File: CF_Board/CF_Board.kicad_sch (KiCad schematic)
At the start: 23 parts, among them J1 Conn_02x04_Odd_Even, SW1 SW_DIP_x08, U1 74FCT16245, U2 74HCT245, U3 22V10, U4 74HCT688, U5 74HCT138, U6 74LVC1G07, X1 DIN41612_03x32_ABC_VMEbus

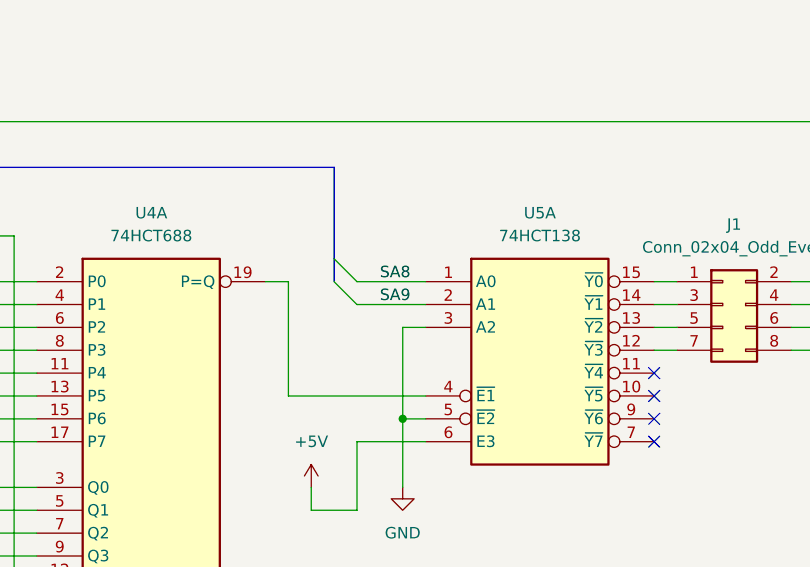
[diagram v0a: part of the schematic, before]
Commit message: Change address decoding to 4KB blocks
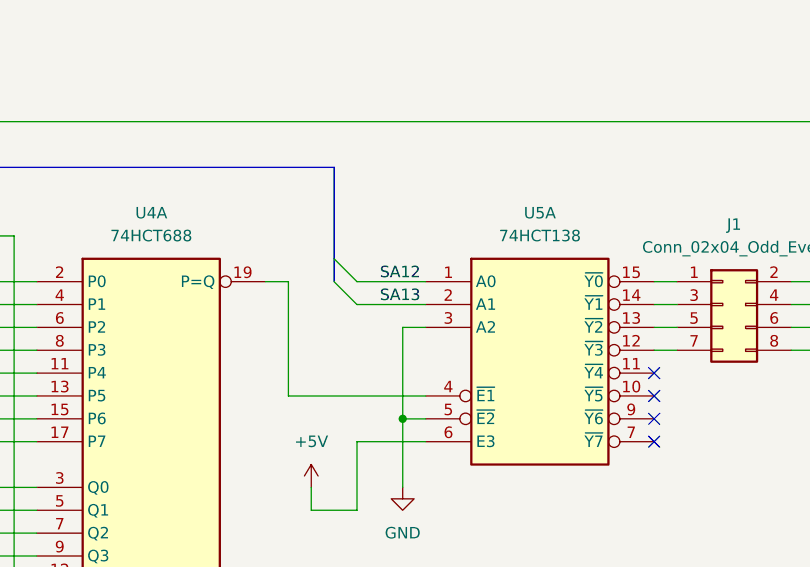
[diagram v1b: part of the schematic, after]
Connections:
- net SA8: no longer U5.1 (A0)
- net SA9: no longer U5.2 (A1)
- new net SA12: U5.1 (A0)
- new net SA13: U5.2 (A1)
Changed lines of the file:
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@@
     (effects (font (size 1.27 1.27)) (justify right bottom))
   )
-  (label "SA9" (at 266.7 167.64 0)
+  (label "SA13" (at 266.7 167.64 0)
     (effects (font (size 1.27 1.27)) (justify left bottom))
   )
@@
     (effects (font (size 1.27 1.27)) (justify left bottom))
   )
-  (label "SA8" (at 266.7 165.1 0)
+  (label "SA12" (at 266.7 165.1 0)
     (effects (font (size 1.27 1.27)) (justify left bottom))
   )

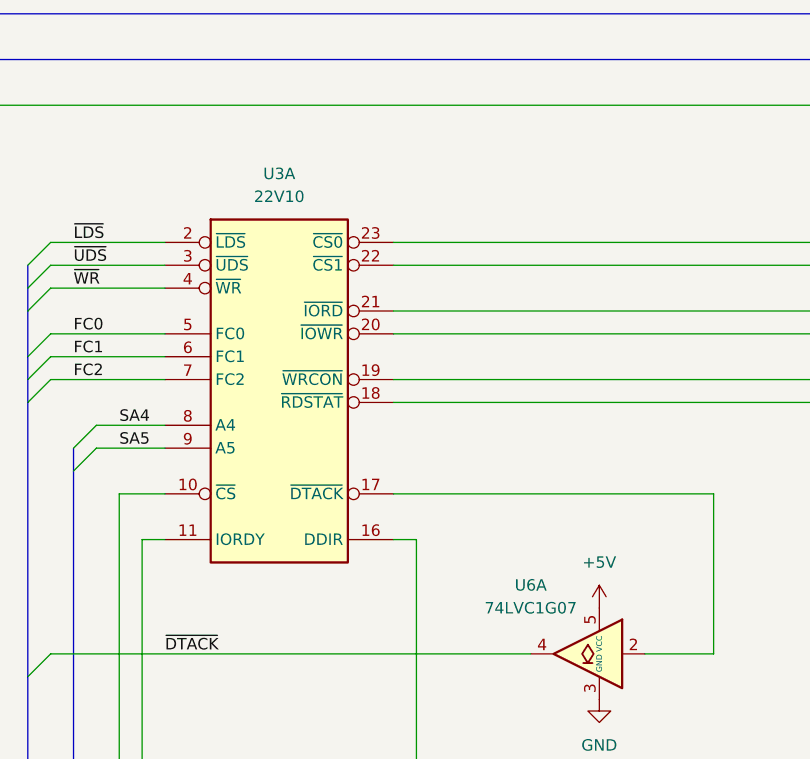
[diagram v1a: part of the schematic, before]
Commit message: Add in-use LED
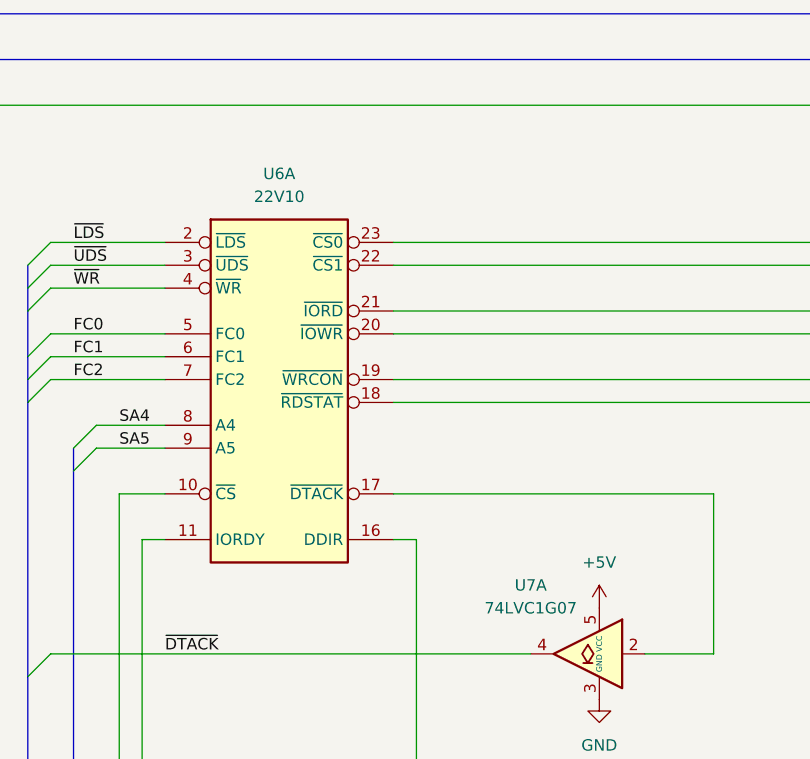
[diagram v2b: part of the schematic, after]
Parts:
- renumbered U3 to U6, U6 to U7
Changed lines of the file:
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@@
   (symbol (lib_id "COMET_symbols:74x1G07") (at 276.86 91.44 0) (mirror y) (unit 1)
     (in_bom yes) (on_board yes)
-    (property "Reference" "U6" (id 0) (at 269.24 83.82 0))
+    (property "Reference" "U7" (id 0) (at 269.24 83.82 0))
     (property "Value" "74LVC1G07" (id 1) (at 269.24 86.36 0))
     (property "Footprint" "COMET_footprints:Package_SOT23-5" (id 2) (at 276.86 91.44 0)
@@
   (symbol (lib_id "CF_Board:22V10") (at 241.3 60.96 0) (unit 1)
     (in_bom yes) (on_board yes) (fields_autoplaced)
-    (property "Reference" "U3" (id 0) (at 241.3 38.1 0))
+    (property "Reference" "U6" (id 0) (at 241.3 38.1 0))
     (property "Value" "22V10" (id 1) (at 241.3 40.64 0))
     (property "Footprint" "Package_DIP:DIP-24_W7.62mm_Socket" (id 2) (at 241.3 68.58 0)
@@
   (symbol (lib_id "COMET_symbols:74x1G07") (at 276.86 91.44 0) (unit 2)
     (in_bom yes) (on_board yes) (fields_autoplaced)
-    (property "Reference" "U6" (id 0) (at 278.13 90.1699 0)
+    (property "Reference" "U7" (id 0) (at 278.13 90.1699 0)
       (effects (font (size 1.27 1.27)) (justify left) hide)
     )
@@
       (reference "#PWR035") (unit 1) (value "+5V") (footprint "")
     )
+    (path "/8c055054-ec87-47ff-a53f-2ab313e3f5a5/a9a15d0f-5372-4367-9eac-932310111a3d"
+      (reference "#PWR036") (unit 1) (value "GND") (footprint "")
+    )
     (path "/8c055054-ec87-47ff-a53f-2ab313e3f5a5/4a3dff2b-a332-4f67-a2b7-a22fe1597ff4"
-      (reference "#PWR036") (unit 1) (value "GND") (footprint "")
+      (reference "#PWR037") (unit 1) (value "GND") (footprint "")
     )
     (path "/8c055054-ec87-47ff-a53f-2ab313e3f5a5/10650d22-6857-40a1-b492-46769c22407b"
-      (reference "#PWR037") (unit 1) (value "+5V") (footprint "")
+      (reference "#PWR038") (unit 1) (value "+5V") (footprint "")
     )
     (path "/8c055054-ec87-47ff-a53f-2ab313e3f5a5/27bb9906-69ce-49c5-b498-0c6583c3f6d3"
-      (reference "#PWR038") (unit 1) (value "GND") (footprint "")
+      (reference "#PWR039") (unit 1) (value "GND") (footprint "")
     )
     (path "/cae18acc-bd78-4da2-b66f-6219bb4579c3"
@@
       (reference "D1") (unit 1) (value "ACT") (footprint "COMET_footprints:LED_SMD0805")
     )
+    (path "/8c055054-ec87-47ff-a53f-2ab313e3f5a5/f82f6d47-c157-4d06-93be-d169a9d1d0db"
+      (reference "D2") (unit 1) (value "IN USE") (footprint "COMET_footprints:LED_SMD0805")
+    )
     (path "/499364ce-bdfc-457a-8aa7-047e56692ab1"
       (reference "J1") (unit 1) (value "Conn_02x04_Odd_Even") (footprint "Connector_PinHeader_2.54mm:PinHeader_2x04_P2.54mm_Vertical")
@@
       (reference "R3") (unit 1) (value "1K") (footprint "COMET_footprints:R_SMD0805")
     )
+    (path "/8c055054-ec87-47ff-a53f-2ab313e3f5a5/31b0cbd2-be15-47c0-8cda-bdc3fd83ce20"
+      (reference "R4") (unit 1) (value "1K") (footprint "COMET_footprints:R_SMD0805")
+    )
     (path "/9581bc50-ee87-45b9-940d-768a95d4e1b1"
       (reference "RN1") (unit 1) (value "R_Pack04") (footprint "Resistor_SMD:R_Cat16-4")
@@
       (reference "U2") (unit 2) (value "74HCT245") (footprint "COMET_footprints:Package_SO20W")
     )
-    (path "/bf78465e-8143-4386-9bea-26a4dc82fef1"
-      (reference "U3") (unit 1) (value "22V10") (footprint "Package_DIP:DIP-24_W7.62mm_Socket")
-    )
     (path "/c69e888b-138f-4719-9a37-3da8c0c6ecc8"
       (reference "U3") (unit 2) (value "22V10") (footprint "Package_DIP:DIP-24_W7.62mm_Socket")
@@
       (reference "U5") (unit 2) (value "74HCT138") (footprint "")
     )
+    (path "/bf78465e-8143-4386-9bea-26a4dc82fef1"
+      (reference "U6") (unit 1) (value "22V10") (footprint "Package_DIP:DIP-24_W7.62mm_Socket")
+    )
     (path "/4ba0c2f3-3832-4528-aeb9-3e5b8717f3f0"
-      (reference "U6") (unit 1) (value "74LVC1G07") (footprint "COMET_footprints:Package_SOT23-5")
+      (reference "U7") (unit 1) (value "74LVC1G07") (footprint "COMET_footprints:Package_SOT23-5")
     )
     (path "/f6922de3-83a8-4ae7-a429-21dcab08499a"
-      (reference "U6") (unit 2) (value "74LVC1G07") (footprint "COMET_footprints:Package_SOT23-5")
+      (reference "U7") (unit 2) (value "74LVC1G07") (footprint "COMET_footprints:Package_SOT23-5")
     )
     (path "/8c055054-ec87-47ff-a53f-2ab313e3f5a5/34e759cd-e28a-4c0c-b576-973f07e5c0f9"
-      (reference "U7") (unit 1) (value "74FCT245") (footprint "COMET_footprints:Package_QSOP20")
+      (reference "U8") (unit 1) (value "74FCT245") (footprint "COMET_footprints:Package_QSOP20")
     )
     (path "/8c055054-ec87-47ff-a53f-2ab313e3f5a5/bcafce73-2c98-40e6-a329-5f4de00f37ef"
-      (reference "U7") (unit 2) (value "74FCT245") (footprint "")
+      (reference "U8") (unit 2) (value "74FCT245") (footprint "")
     )
     (path "/8c055054-ec87-47ff-a53f-2ab313e3f5a5/f384fbd4-38b0-4ed2-a372-5d3477c371e4"
-      (reference "U8") (unit 1) (value "74HCT74") (footprint "COMET_footprints:Package_SO14")
+      (reference "U9") (unit 1) (value "74HCT74") (footprint "COMET_footprints:Package_SO14")
     )
     (path "/8c055054-ec87-47ff-a53f-2ab313e3f5a5/2d309f4c-163d-4028-9c71-ba1623007e1a"
-      (reference "U8") (unit 2) (value "74HCT74") (footprint "COMET_footprints:Package_SO14")
+      (reference "U9") (unit 2) (value "74HCT74") (footprint "COMET_footprints:Package_SO14")
     )
     (path "/8c055054-ec87-47ff-a53f-2ab313e3f5a5/801c220f-f363-4e5b-beeb-548acd8f298d"
-      (reference "U8") (unit 3) (value "74HCT74") (footprint "COMET_footprints:Package_SO14")
+      (reference "U9") (unit 3) (value "74HCT74") (footprint "COMET_footprints:Package_SO14")
     )
     (path "/8c055054-ec87-47ff-a53f-2ab313e3f5a5/80aecc33-2700-4f84-867e-e95febb524d7"
-      (reference "U9") (unit 1) (value "74HCT245") (footprint "COMET_footprints:Package_SO20W")
+      (reference "U10") (unit 1) (value "74HCT245") (footprint "COMET_footprints:Package_SO20W")
     )
     (path "/8c055054-ec87-47ff-a53f-2ab313e3f5a5/301e26e0-2284-4361-8a21-cdfab701578e"
-      (reference "U9") (unit 2) (value "74HCT245") (footprint "COMET_footprints:Package_SO20W")
+      (reference "U10") (unit 2) (value "74HCT245") (footprint "COMET_footprints:Package_SO20W")
     )
     (path "/8c055054-ec87-47ff-a53f-2ab313e3f5a5/ee0c1982-1d2f-46f0-8b26-f0ced053c93e"
-      (reference "U10") (unit 1) (value "74HCT245") (footprint "COMET_footprints:Package_SO20W")
+      (reference "U11") (unit 1) (value "74HCT245") (footprint "COMET_footprints:Package_SO20W")
     )
     (path "/8c055054-ec87-47ff-a53f-2ab313e3f5a5/06c64bbc-cc23-465a-8aca-8c908bcb46f0"
-      (reference "U10") (unit 2) (value "74HCT245") (footprint "COMET_footprints:Package_SO20W")
+      (reference "U11") (unit 2) (value "74HCT245") (footprint "COMET_footprints:Package_SO20W")
     )
     (path "/8c055054-ec87-47ff-a53f-2ab313e3f5a5/5822f788-16e3-4f95-a414-c1f2b160c11c"
-      (reference "U11") (unit 1) (value "74LVC1G08") (footprint "COMET_footprints:Package_SOT23-5")
+      (reference "U12") (unit 1) (value "74LVC1G08") (footprint "COMET_footprints:Package_SOT23-5")
     )
     (path "/8c055054-ec87-47ff-a53f-2ab313e3f5a5/d913847b-a0a4-4a07-b5e1-a62a38846430"
-      (reference "U11") (unit 2) (value "74LVC1G08") (footprint "COMET_footprints:Package_SOT23-5")
+      (reference "U12") (unit 2) (value "74LVC1G08") (footprint "COMET_footprints:Package_SOT23-5")
     )
     (path "/8c055054-ec87-47ff-a53f-2ab313e3f5a5/0be3b92c-3373-4b1a-973e-16062d14b9e8"
-      (reference "U12") (unit 1) (value "74LVC1G32") (footprint "COMET_footprints:Package_SOT23-5")
+      (reference "U13") (unit 1) (value "74LVC1G32") (footprint "COMET_footprints:Package_SOT23-5")
     )
     (path "/8c055054-ec87-47ff-a53f-2ab313e3f5a5/633e274d-81e8-4dd7-9d8d-233aa0deb5f6"
-      (reference "U12") (unit 2) (value "74LVC1G32") (footprint "COMET_footprints:Package_SOT23-5")
+      (reference "U13") (unit 2) (value "74LVC1G32") (footprint "COMET_footprints:Package_SOT23-5")
     )
     (path "/af791db5-c55d-4390-9b8d-c57620a9ba6f"
